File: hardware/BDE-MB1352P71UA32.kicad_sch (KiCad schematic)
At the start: 11 parts, among them J401 Conn_ARM_JTAG_SWD_10, SW401 SW_Push, U401 BDE-MB1352P71UA32, U402 USBLC6-2P6, U403 USBLC6-2P6

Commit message: reannotate
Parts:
- renumbered C401 to C301, C402 to C302, C403 to C303, D401 to D301, J401 to J301, R401 to R301, R402 to R302, SW401 to SW301, U401 to U301, U402 to U302, U403 to U303
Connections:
- no-connect marks 20 -> 21
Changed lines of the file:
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@@
+	)
+	(no_connect
+		(at 166.37 105.41)
 	)
 	(no_connect
@@
 		(dnp no)
 		(fields_autoplaced yes)
-		(property "Reference" "#PWR0411"
+		(property "Reference" "#PWR0311"
 			(at 142.24 143.51 0)
 			(effects
@@
 			(project "Senior_Design"
 				(path "/8f5928e8-0fc1-4443-a20f-3bfeb956761e/dd2813e4-a810-44d7-8b7e-d46ce1c3fa30"
-					(reference "#PWR0411")
+					(reference "#PWR0311")
 					(unit 1)
 				)
@@
 		(dnp no)
 		(fields_autoplaced yes)
-		(property "Reference" "#PWR0406"
+		(property "Reference" "#PWR0306"
 			(at 152.4 78.74 0)
 			(effects
@@
 			(project "Senior_Design"
 				(path "/8f5928e8-0fc1-4443-a20f-3bfeb956761e/dd2813e4-a810-44d7-8b7e-d46ce1c3fa30"
-					(reference "#PWR0406")
+					(reference "#PWR0306")
 					(unit 1)
 				)
@@
 		(on_board yes)
 		(dnp no)
-		(property "Reference" "U403"
+		(property "Reference" "U303"
 			(at 135.89 138.684 0)
 			(effects
@@
 			(project "Senior_Design"
 				(path "/8f5928e8-0fc1-4443-a20f-3bfeb956761e/dd2813e4-a810-44d7-8b7e-d46ce1c3fa30"
-					(reference "U403")
+					(reference "U303")
 					(unit 1)
 				)
@@
 		(dnp no)
 		(fields_autoplaced yes)
-		(property "Reference" "#PWR0405"
+		(property "Reference" "#PWR0305"
 			(at 129.54 78.74 0)
 			(effects
@@
 			(project "Senior_Design"
 				(path "/8f5928e8-0fc1-4443-a20f-3bfeb956761e/dd2813e4-a810-44d7-8b7e-d46ce1c3fa30"
-					(reference "#PWR0405")
+					(reference "#PWR0305")
 					(unit 1)
 				)
@@
 		(on_board yes)
 		(dnp no)
-		(property "Reference" "C401"
+		(property "Reference" "C301"
 			(at 222.758 50.546 0)
 			(effects
@@
 			(project "Senior_Design"
 				(path "/8f5928e8-0fc1-4443-a20f-3bfeb956761e/dd2813e4-a810-44d7-8b7e-d46ce1c3fa30"
-					(reference "C401")
+					(reference "C301")
 					(unit 1)
 				)
@@
 		(dnp no)
 		(fields_autoplaced yes)
-		(property "Reference" "J401"
+		(property "Reference" "J301"
 			(at 64.77 99.0599 0)
 			(effects
@@
 			(project "Senior_Design"
 				(path "/8f5928e8-0fc1-4443-a20f-3bfeb956761e/dd2813e4-a810-44d7-8b7e-d46ce1c3fa30"
-					(reference "J401")
+					(reference "J301")
 					(unit 1)
 				)
@@
 		(on_board yes)
 		(dnp no)
-		(property "Reference" "U402"
+		(property "Reference" "U302"
 			(at 99.06 139.192 0)
 			(effects
@@
 			(project "Senior_Design"
 				(path "/8f5928e8-0fc1-4443-a20f-3bfeb956761e/dd2813e4-a810-44d7-8b7e-d46ce1c3fa30"
-					(reference "U402")
+					(reference "U302")
 					(unit 1)
 				)
@@
 		(dnp no)
 		(fields_autoplaced yes)
-		(property "Reference" "#PWR0409"
+		(property "Reference" "#PWR0309"
 			(at 76.2 124.46 0)
 			(effects
@@
 			(project "Senior_Design"
 				(path "/8f5928e8-0fc1-4443-a20f-3bfeb956761e/dd2813e4-a810-44d7-8b7e-d46ce1c3fa30"
-					(reference "#PWR0409")
+					(reference "#PWR0309")
 					(unit 1)
 				)
@@
 		(on_board yes)
 		(dnp no)
-		(property "Reference" "C403"
+		(property "Reference" "C303"
 			(at 148.59 68.326 0)
 			(effects
@@
 			(project "Senior_Design"
 				(path "/8f5928e8-0fc1-4443-a20f-3bfeb956761e/dd2813e4-a810-44d7-8b7e-d46ce1c3fa30"
-					(reference "C403")
+					(reference "C303")
 					(unit 1)
 				)
@@
 		(dnp no)
 		(fields_autoplaced yes)
-		(property "Reference" "#PWR0404"
+		(property "Reference" "#PWR0304"
 			(at 140.97 76.2 0)
 			(effects
@@
 			(project "Senior_Design"
 				(path "/8f5928e8-0fc1-4443-a20f-3bfeb956761e/dd2813e4-a810-44d7-8b7e-d46ce1c3fa30"
-					(reference "#PWR0404")
+					(reference "#PWR0304")
 					(unit 1)
 				)
@@
 		(dnp no)
 		(fields_autoplaced yes)
-		(property "Reference" "#PWR0410"
+		(property "Reference" "#PWR0310"
 			(at 105.41 143.51 0)
 			(effects
@@
 			(project "Senior_Design"
 				(path "/8f5928e8-0fc1-4443-a20f-3bfeb956761e/dd2813e4-a810-44d7-8b7e-d46ce1c3fa30"
-					(reference "#PWR0410")
+					(reference "#PWR0310")
 					(unit 1)
 				)
@@
 		(dnp no)
 		(fields_autoplaced yes)
-		(property "Reference" "U401"
+		(property "Reference" "U301"
 			(at 189.23 49.53 0)
 			(effects
@@
 			(project "Senior_Design"
 				(path "/8f5928e8-0fc1-4443-a20f-3bfeb956761e/dd2813e4-a810-44d7-8b7e-d46ce1c3fa30"
-					(reference "U401")
+					(reference "U301")
 					(unit 1)
 				)
@@
 		(dnp no)
 		(fields_autoplaced yes)
-		(property "Reference" "#PWR0402"
+		(property "Reference" "#PWR0302"
 			(at 140.97 53.34 0)
 			(effects
@@
 			(project "Senior_Design"
 				(path "/8f5928e8-0fc1-4443-a20f-3bfeb956761e/dd2813e4-a810-44d7-8b7e-d46ce1c3fa30"
-					(reference "#PWR0402")
+					(reference "#PWR0302")
 					(unit 1)
 				)
@@
 		(dnp no)
 		(fields_autoplaced yes)
-		(property "Reference" "SW401"
+		(property "Reference" "SW301"
 			(at 120.65 54.61 0)
 			(effects
@@
 			(project "Senior_Design"
 				(path "/8f5928e8-0fc1-4443-a20f-3bfeb956761e/dd2813e4-a810-44d7-8b7e-d46ce1c3fa30"
-					(reference "SW401")
+					(reference "SW301")
 					(unit 1)
 				)
@@
 		(dnp no)
 		(fields_autoplaced yes)
-		(property "Reference" "#PWR0407"
+		(property "Reference" "#PWR0307"
 			(at 76.2 83.82 0)
 			(effects
@@
 			(project "Senior_Design"
 				(path "/8f5928e8-0fc1-4443-a20f-3bfeb956761e/dd2813e4-a810-44d7-8b7e-d46ce1c3fa30"
-					(reference "#PWR0407")
+					(reference "#PWR0307")
 					(unit 1)
 				)
@@
 		(on_board yes)
 		(dnp no)
-		(property "Reference" "D401"
+		(property "Reference" "D301"
 			(at 127 68.2626 90)
 			(effects
@@
 			(project "Senior_Design"
 				(path "/8f5928e8-0fc1-4443-a20f-3bfeb956761e/dd2813e4-a810-44d7-8b7e-d46ce1c3fa30"
-					(reference "D401")
+					(reference "D301")
 					(unit 1)
 				)
@@
 		(dnp no)
 		(fields_autoplaced yes)
-		(property "Reference" "#PWR0408"
+		(property "Reference" "#PWR0308"
 			(at 213.36 120.65 0)
 			(effects
@@
 			(project "Senior_Design"
 				(path "/8f5928e8-0fc1-4443-a20f-3bfeb956761e/dd2813e4-a810-44d7-8b7e-d46ce1c3fa30"
-					(reference "#PWR0408")
+					(reference "#PWR0308")
 					(unit 1)
 				)
@@
 		(dnp no)
 		(fields_autoplaced yes)
-		(property "Reference" "#PWR0403"
+		(property "Reference" "#PWR0303"
 			(at 115.57 69.85 0)
 			(effects
@@
 			(project "Senior_Design"
 				(path "/8f5928e8-0fc1-4443-a20f-3bfeb956761e/dd2813e4-a810-44d7-8b7e-d46ce1c3fa30"
-					(reference "#PWR0403")
+					(reference "#PWR0303")
 					(unit 1)
 				)
@@
 		(dnp no)
 		(fields_autoplaced yes)
-		(property "Reference" "C402"
+		(property "Reference" "C302"
 			(at 236.22 50.7999 0)
 			(effects
@@
 			(project "Senior_Design"
 				(path "/8f5928e8-0fc1-4443-a20f-3bfeb956761e/dd2813e4-a810-44d7-8b7e-d46ce1c3fa30"
-					(reference "C402")
+					(reference "C302")
 					(unit 1)
 				)
@@
 		(dnp no)
 		(fields_autoplaced yes)
-		(property "Reference" "#PWR0412"
+		(property "Reference" "#PWR0312"
 			(at 105.41 158.75 0)
 			(effects
@@
 			(project "Senior_Design"
 				(path "/8f5928e8-0fc1-4443-a20f-3bfeb956761e/dd2813e4-a810-44d7-8b7e-d46ce1c3fa30"
-					(reference "#PWR0412")
+					(reference "#PWR0312")
 					(unit 1)
 				)
@@
 		(on_board yes)
 		(dnp no)
-		(property "Reference" "R401"
+		(property "Reference" "R301"
 			(at 143.51 54.6099 0)
 			(effects
@@
 			(project "Senior_Design"
 				(path "/8f5928e8-0fc1-4443-a20f-3bfeb956761e/dd2813e4-a810-44d7-8b7e-d46ce1c3fa30"
-					(reference "R401")
+					(reference "R301")
 					(unit 1)
 				)
@@
 		(dnp no)
 		(fields_autoplaced yes)
-		(property "Reference" "#PWR0413"
+		(property "Reference" "#PWR0313"
 			(at 142.24 158.75 0)
 			(effects
@@
 			(project "Senior_Design"
 				(path "/8f5928e8-0fc1-4443-a20f-3bfeb956761e/dd2813e4-a810-44d7-8b7e-d46ce1c3fa30"
-					(reference "#PWR0413")
+					(reference "#PWR0313")
 					(unit 1)
 				)
@@
 		(on_board yes)
 		(dnp no)
-		(property "Reference" "R402"
+		(property "Reference" "R302"
 			(at 145.796 77.216 0)
 			(effects
@@
 			(project "Senior_Design"
 				(path "/8f5928e8-0fc1-4443-a20f-3bfeb956761e/dd2813e4-a810-44d7-8b7e-d46ce1c3fa30"
-					(reference "R402")
+					(reference "R302")
 					(unit 1)
 				)
@@
 		(on_board yes)
 		(dnp no)
-		(property "Reference" "#FLG0401"
+		(property "Reference" "#FLG0301"
 			(at 213.36 48.895 0)
 			(effects
@@
 			(project "Senior_Design"
 				(path "/8f5928e8-0fc1-4443-a20f-3bfeb956761e/dd2813e4-a810-44d7-8b7e-d46ce1c3fa30"
-					(reference "#FLG0401")
+					(reference "#FLG0301")
 					(unit 1)
 				)
@@
 		(dnp no)
 		(fields_autoplaced yes)
-		(property "Reference" "#PWR0401"
+		(property "Reference" "#PWR0301"
 			(at 232.41 49.53 0)
 			(effects
@@
 			(project "Senior_Design"
 				(path "/8f5928e8-0fc1-4443-a20f-3bfeb956761e/dd2813e4-a810-44d7-8b7e-d46ce1c3fa30"
-					(reference "#PWR0401")
+					(reference "#PWR0301")
 					(unit 1)
 				)

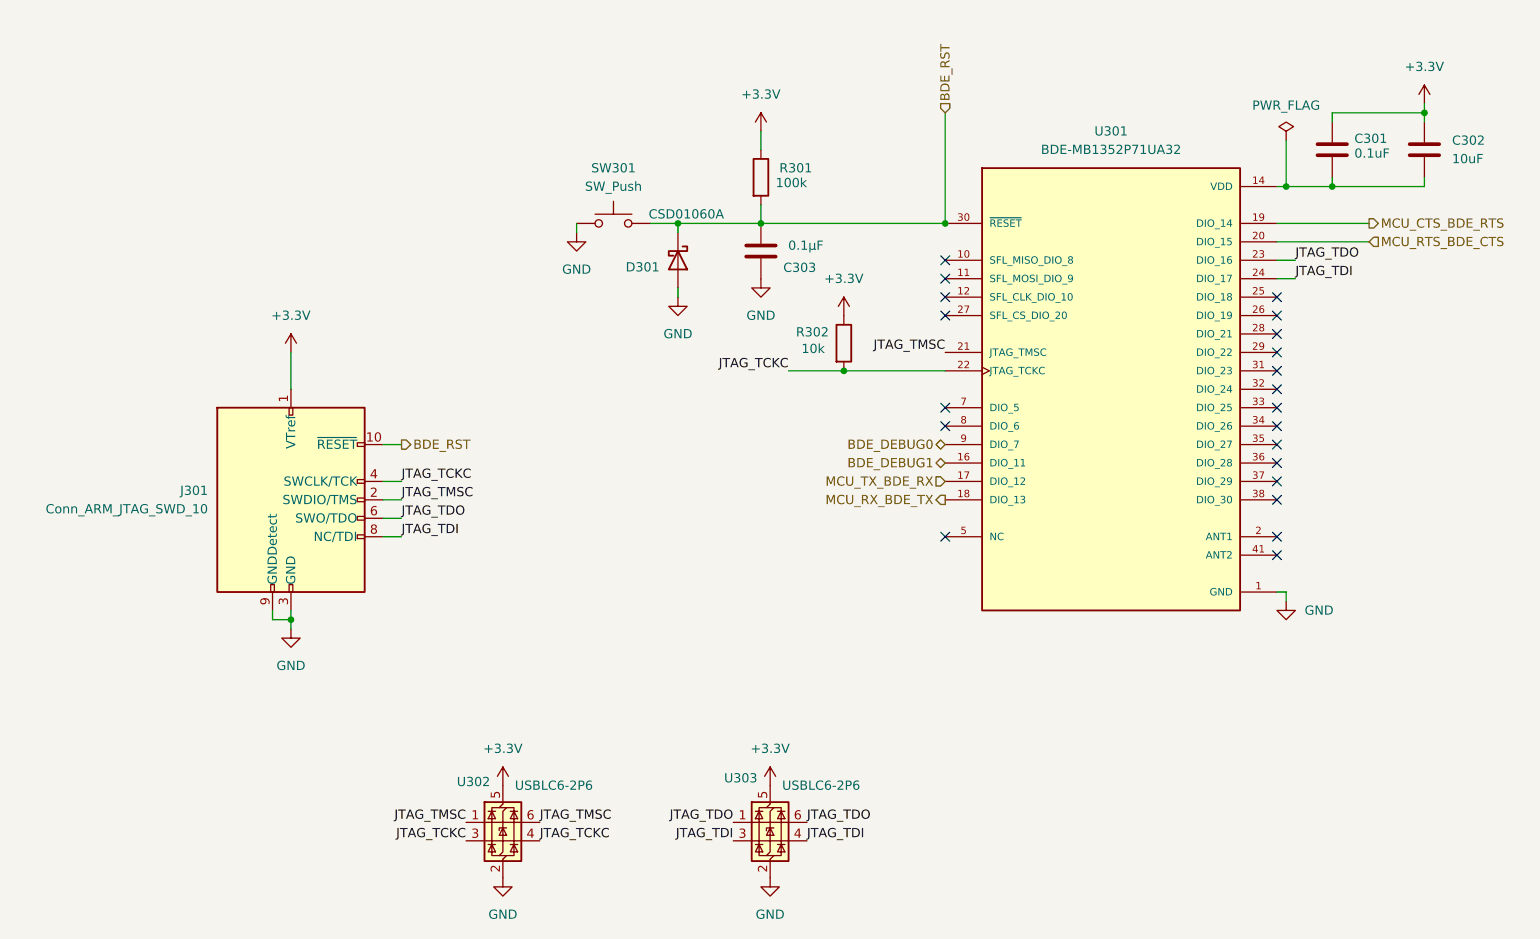
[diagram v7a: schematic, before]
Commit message: added QON pushbutton
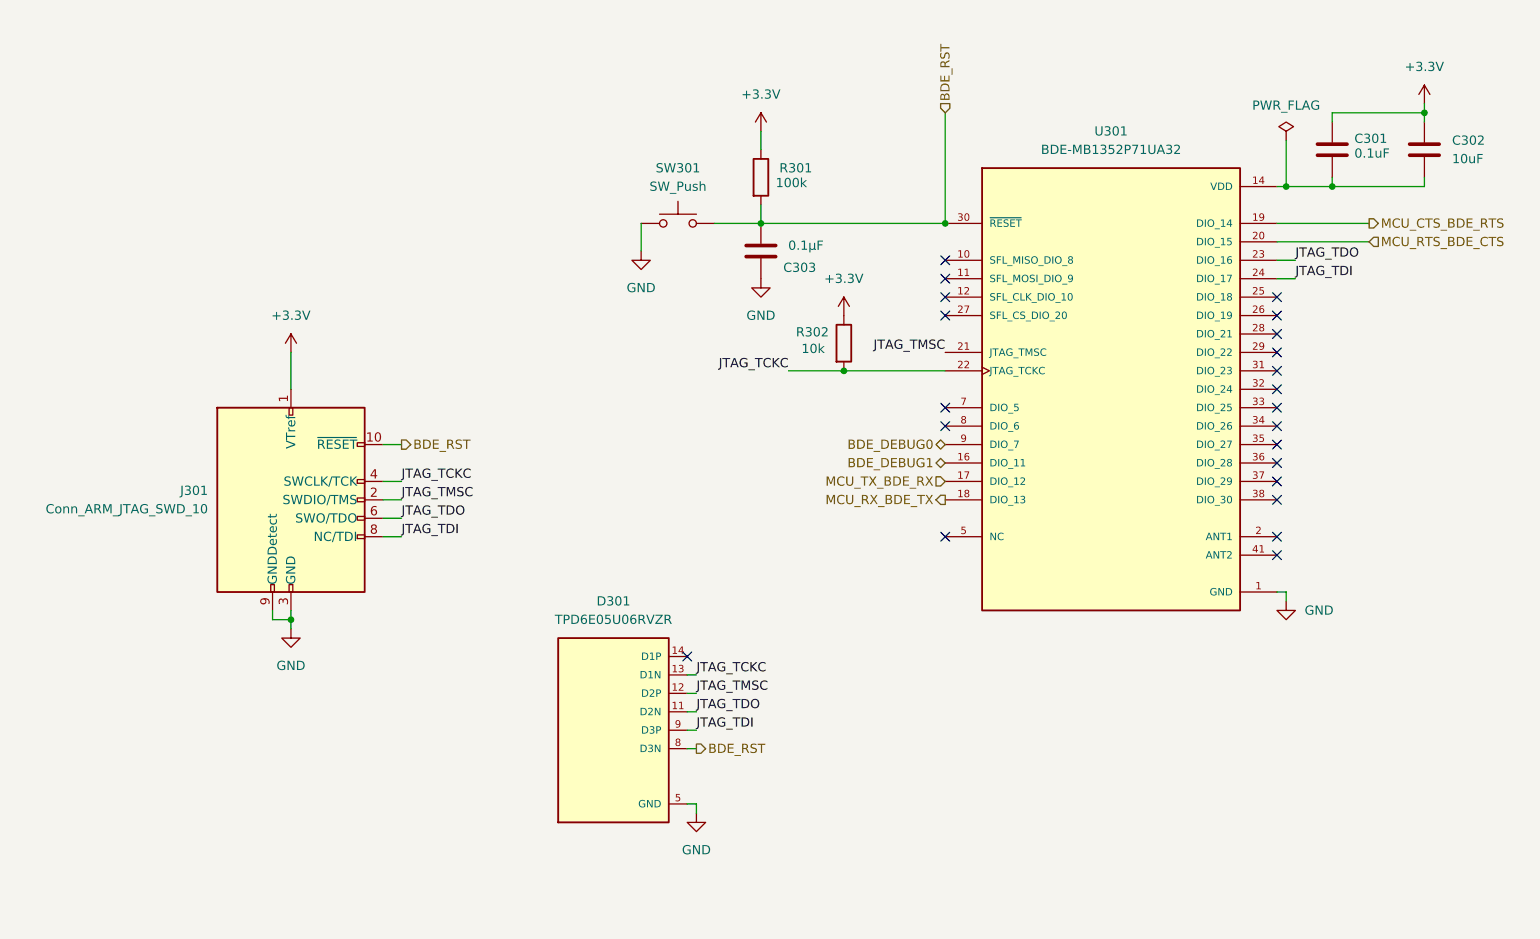
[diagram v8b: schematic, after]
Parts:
- removed D301: CSD01060A, Diode_SMD:D_SOD-123, symbol Diode:CSD01060A
- removed U302, U303: USBLC6-2P6, Package_TO_SOT_SMD:SOT-666, symbol Power_Protection:USBLC6-2P6
- added D301: TPD6E05U06RVZR, pyronet_footprints:SON50P135X350X55-14N, symbol pyronet_symbols:TPD6E05U06RVZR
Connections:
- net BDE_RST: now also D301.8 (D3N)
- net GND: now also D301.10 (GND), D301.5 (GND)
- net JTAG_TCKC: now also D301.13 (D1N)
- net JTAG_TDI: now also D301.9 (D3P)
- net JTAG_TDO: now also D301.11 (D2N)
- net JTAG_TMSC: now also D301.12 (D2P)
- no-connect marks 21 -> 22
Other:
- moved on the sheet: SW301
